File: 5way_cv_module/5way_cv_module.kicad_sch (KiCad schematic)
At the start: 0 parts

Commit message: updates
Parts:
- added C1: 10uF, Capacitor_SMD:C_0201_0603Metric, symbol Device:C_Small
- added C2, C3: 1uF, Capacitor_SMD:C_0201_0603Metric, symbol Device:C_Small
- added D1: LL4148, Diode_SMD:D_MiniMELF, symbol Device:D_Small
- added J1: I/O connector, symbol cycfi_library:conn_1x3
- added J2: 5-way Switch Connector, symbol cycfi_library:conn_1x4
- added R1, R2: 3k, symbol Device:R_Small
- added R3, R4: 1.5k, symbol Device:R_Small
- added U1: HT7550-1, symbol cycfi_library:sot89-3-gio
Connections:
- new net: C2.1, D1.1 (K), U1.2 (IN)
- new net 5v: C3.1, R1.1, R3.1, U1.3 (OUT)
- new net GND: C1.2, C2.2, C3.2, J1.2 (P2), R2.2, R4.2, U1.1 (GND)
- new net V+: D1.2 (A), J1.1 (P1)
- new net bridge: J2.3 (P3), R4.1
- new net common: C1.1, J1.3 (P3), J2.4 (P4)
- new net middle: J2.2 (P2), R1.2, R2.1
- new net neck: J2.1 (P1), R3.2
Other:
- note added: "1 2 3 4 5"
- note added: "5v 3.3v 2.5v 1.25v 0v"
- note added: "Connectors"
- note added: "Output"
- note added: "Position"
- note added: "Voltage Divider"
- note added: "Voltage Regulator"

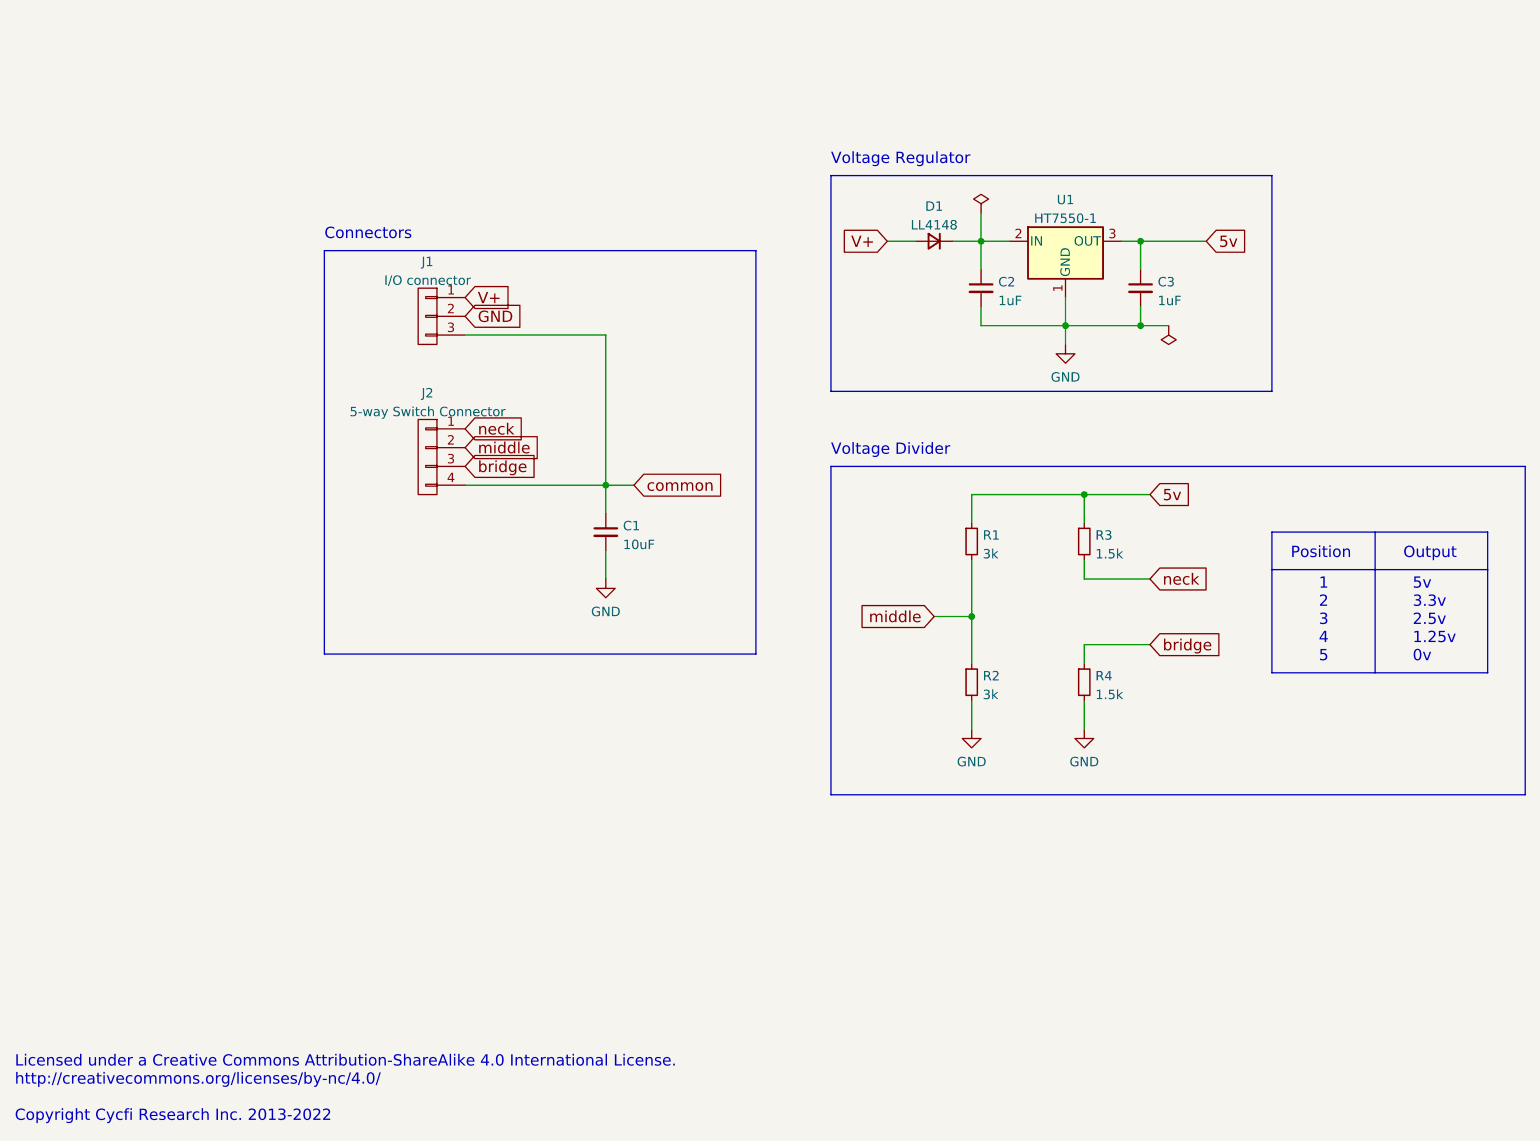
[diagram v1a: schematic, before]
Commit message: added opamp buffer better layout
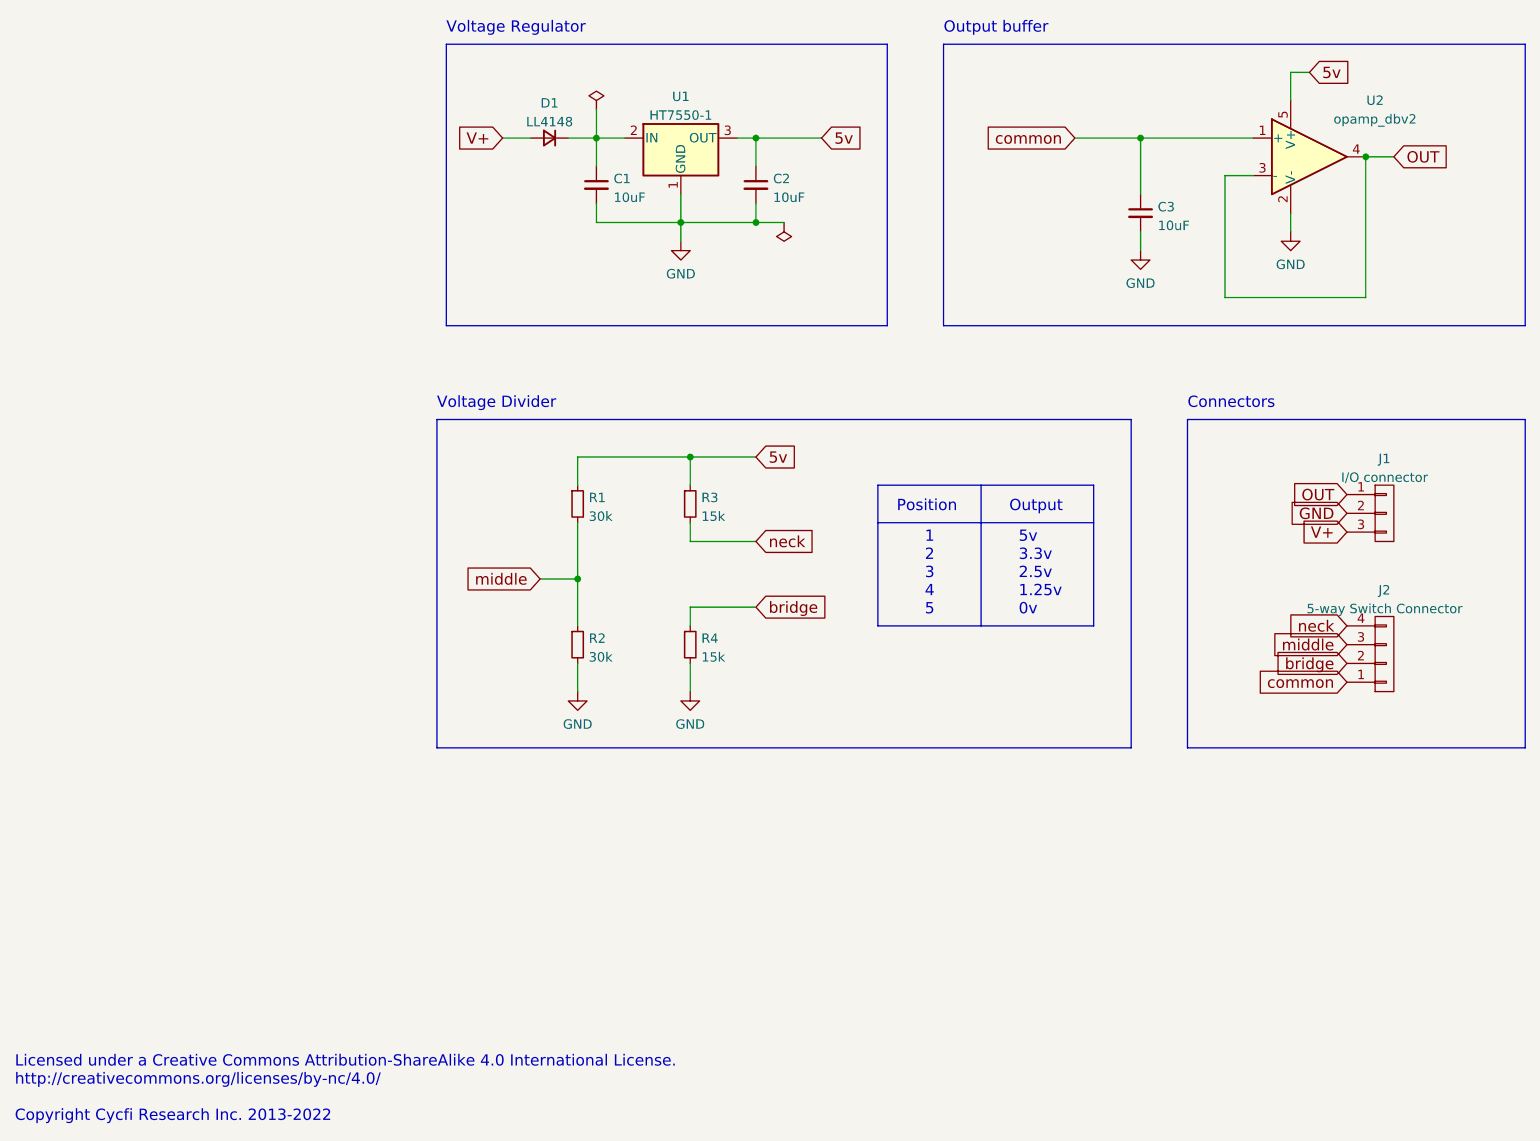
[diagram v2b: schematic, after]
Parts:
- removed C1: 10uF, Capacitor_SMD:C_0201_0603Metric, symbol Device:C_Small
- added C3: 10uF, Capacitor_SMD:C_0603_1608Metric, symbol Device:C_Small
- added U2: opamp_dbv2, Package_TO_SOT_SMD:SOT-23-5, symbol cycfi_library:opamp_dbv2
- C1: renamed from C2; value 1uF -> 10uF; footprint Capacitor_SMD:C_0201_0603Metric -> Capacitor_SMD:C_0603_1608Metric
- C2: renamed from C3; value 1uF -> 10uF; footprint Capacitor_SMD:C_0201_0603Metric -> Capacitor_SMD:C_0603_1608Metric
- J1: footprint (none) -> cycfi_library:pin_header_1x3p_2.54mm_smd_horizontal
- J2: footprint (none) -> cycfi_library:pin_socket_1x4p_2.54mm_smd_horizontal
- R1, R2: value 3k -> 30k; footprint (none) -> Resistor_SMD:R_0402_1005Metric
- R3, R4: value 1.5k -> 15k; footprint (none) -> Resistor_SMD:R_0402_1005Metric
- U1: footprint (none) -> Package_TO_SOT_SMD:SOT-89-3
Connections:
- net 5v: now also U2.5 (V+)
- net GND: now also C3.2, U2.2 (V-)
- net V+: now also J1.3 (P3); no longer J1.1 (P1)
- net bridge: now also J2.2 (P2); no longer J2.3 (P3)
- net common: now also J2.1 (P1), C3.1, U2.1 (+); no longer J1.3 (P3), J2.4 (P4)
- net middle: now also J2.3 (P3); no longer J2.2 (P2)
- net neck: now also J2.4 (P4); no longer J2.1 (P1)
- new net OUT: J1.1 (P1), U2.3 (-), U2.4
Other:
- note added: "Output buffer"
- moved on the sheet: C1, C2, D1, J1, J2, R1, R2, R3, R4, U1
